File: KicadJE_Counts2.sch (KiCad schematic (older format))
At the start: 40 parts, among them J201 clk_in, J202 clk_out, J203 Hold, J204 Reset, J205 Slave clock sel, P201 HEADER_2x5_Doepfer, U201 LM555, U202 4017

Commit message: counter fine
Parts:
- removed C201: 22u, Capacitor_SMD:C_1206_3216Metric_Pad1.42x1.75mm_HandSolder, symbol Device:C
- removed C202: 10n, AJ:C_0805_AJ, symbol Device:C
- removed R201: 3k3, AJ:R_0805_AJ, symbol Device:R
- removed R202: 220k, AJ:R_0805_AJ, symbol Device:R
- removed RV201: 50k Rate, Connector_JST:JST_EH_B3B-EH-A_1x03_P2.50mm_Vertical, symbol Device:R_POT
- removed U201: LM555, AJ-Dropbox-Kicad:AJ_SO-8_5.3x6.2mm_P1.27mm, symbol KicadJE_SympleSeq-rescue:LM555-Timer
- added C?: 10n, Capacitor_SMD:C_0805_2012Metric_Pad1.15x1.40mm_HandSolder, symbol Device:C
- added C?: 10u, Capacitor_SMD:C_0805_2012Metric_Pad1.15x1.40mm_HandSolder, symbol Device:C
- added R?: 3k3, Resistor_SMD:R_0805_2012Metric_Pad1.15x1.40mm_HandSolder, symbol Device:R
- added R?: 220k, Resistor_SMD:R_0805_2012Metric_Pad1.15x1.40mm_HandSolder, symbol Device:R
- added RV?: 50k_freq, Potentiometer_THT:Potentiometer_China_RK09_Single_Vertical_AJ, symbol Device:R_POT
- added U?: LM555, AJ-Dropbox-Kicad:AJ_SO-8_5.3x6.2mm_P1.27mm, symbol KicadJE_Counts-rescue:LM555-Timer
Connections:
- net labels added: GNDS
- wire segments 166 -> 168
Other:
- moved on the sheet: C203, C204, C205, C206, C207, D201, D202, D203, D204, D205, D206, D207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

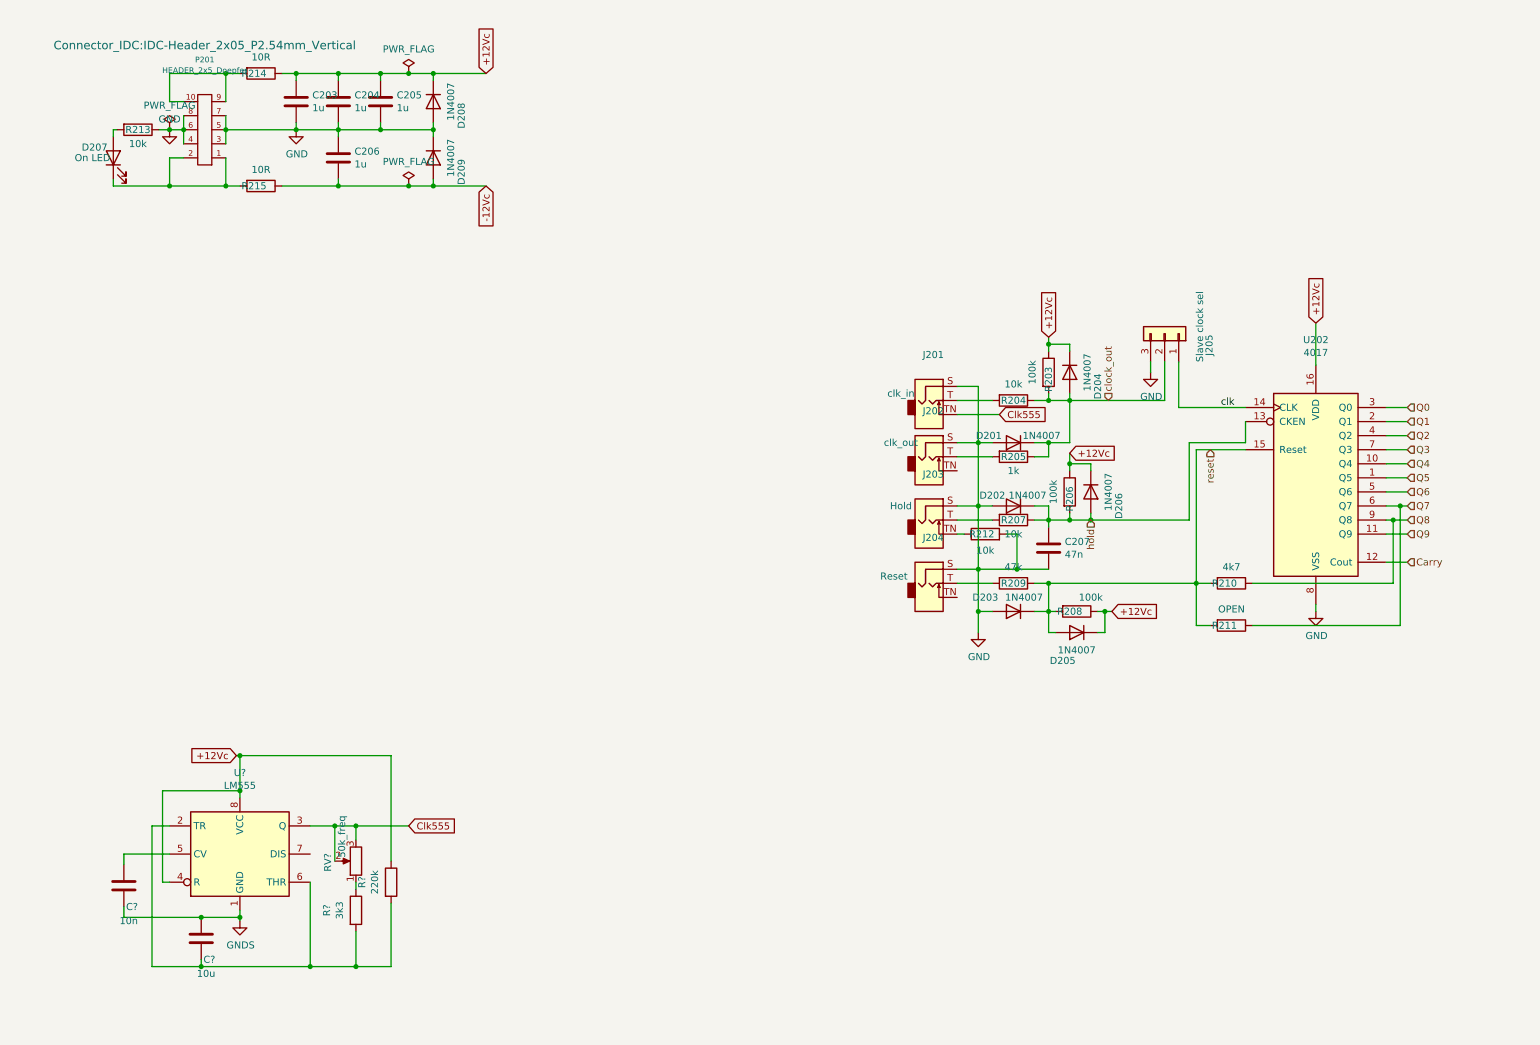
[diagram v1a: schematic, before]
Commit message: distortion added as count2
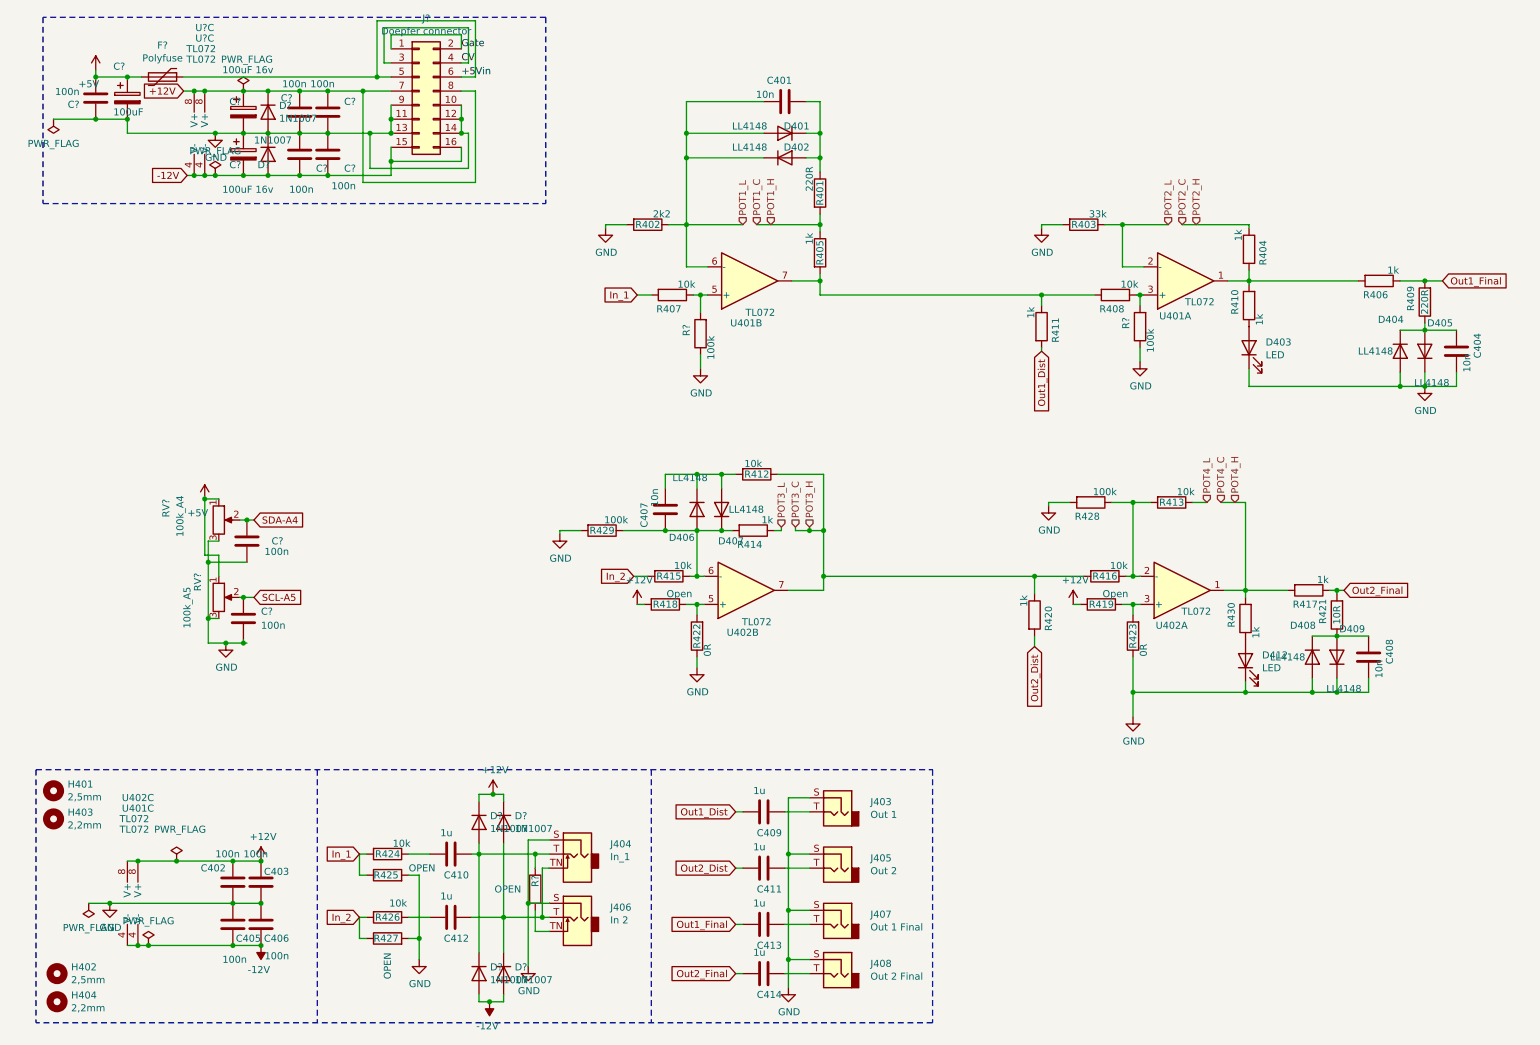
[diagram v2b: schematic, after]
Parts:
- removed C203, C205: 1u, AJ:C_0805_AJ, symbol Device:C
- removed C204, C206: 1u, Capacitor_SMD:C_1206_3216Metric_Pad1.42x1.75mm_HandSolder, symbol Device:C
- removed C207: 47n, AJ:C_0805_AJ, symbol Device:C
- removed C?: 10n, Capacitor_SMD:C_0805_2012Metric_Pad1.15x1.40mm_HandSolder, symbol Device:C
- removed C?: 10u, Capacitor_SMD:C_0805_2012Metric_Pad1.15x1.40mm_HandSolder, symbol Device:C
- removed D201, D202, D203, D204, D205, D206, D208, D209: 1N4007, Diode_SMD:D_MiniMELF, symbol Diode:LL4148
- removed D207: On LED, AJ:D_0805_AJ, symbol Device:LED
- removed J201: clk_in, Connector_Audio:Jack_3.5mm_Ledino_KB3SPRS_Horizontal, symbol Connector:AudioJack2_SwitchT
- removed J202: clk_out, Connector_Audio:Jack_3.5mm_Ledino_KB3SPRS_Horizontal, symbol Connector:AudioJack2_SwitchT
- removed J203: Hold, Connector_Audio:Jack_3.5mm_Ledino_KB3SPRS_Horizontal, symbol Connector:AudioJack2_SwitchT
- removed J204: Reset, Connector_Audio:Jack_3.5mm_Ledino_KB3SPRS_Horizontal, symbol Connector:AudioJack2_SwitchT
- removed J205: Slave clock sel, Connector_PinHeader_2.54mm:PinHeader_1x03_P2.54mm_Vertical, symbol Connector_Generic:Conn_01x03
- removed P201: HEADER_2x5_Doepfer, Connector_IDC:IDC-Header_2x05_P2.54mm_Vertical, symbol Eurorack:HEADER_2x5_Doepfer
- removed R203, R206, R208: 100k, AJ:R_0805_AJ, symbol Device:R
- removed R204, R207, R212, R213: 10k, AJ:R_0805_AJ, symbol Device:R
- removed R205: 1k, AJ:R_0805_AJ, symbol Device:R
- removed R209: 47k, AJ:R_0805_AJ, symbol Device:R
- removed R210: 4k7, AJ:R_0805_AJ, symbol Device:R
- removed R211: OPEN, AJ:R_0805_AJ, symbol Device:R
- removed R214, R215: 10R, AJ:R_0805_AJ, symbol Device:R
- removed R?: 3k3, Resistor_SMD:R_0805_2012Metric_Pad1.15x1.40mm_HandSolder, symbol Device:R
- removed R?: 220k, Resistor_SMD:R_0805_2012Metric_Pad1.15x1.40mm_HandSolder, symbol Device:R
- removed RV?: 50k_freq, Potentiometer_THT:Potentiometer_China_RK09_Single_Vertical_AJ, symbol Device:R_POT
- removed U202: 4017, AJ:SOIC-16_4.55x10.3mm_P1.27mm, symbol 4xxx:4017
- removed U?: LM555, AJ-Dropbox-Kicad:AJ_SO-8_5.3x6.2mm_P1.27mm, symbol KicadJE_Counts-rescue:LM555-Timer
- added C401, C404, C407, C408: 10n, Capacitor_SMD:C_0805_2012Metric_Pad1.15x1.40mm_HandSolder, symbol Device:C
- added C402, C403, C405, C406, C? (x7): 100n, Capacitor_SMD:C_0805_2012Metric_Pad1.15x1.40mm_HandSolder, symbol Device:C
- added C409, C410, C411, C412, C413, C414: 1u, Capacitor_SMD:C_0805_2012Metric_Pad1.15x1.40mm_HandSolder, symbol Device:C
- added C? (x2): 100uF 16v, Capacitor_THT:CP_Radial_D5.0mm_P2.50mm, symbol Device:CP
- added C?: 100uF, Capacitor_THT:CP_Radial_D5.0mm_P2.50mm, symbol Device:CP
- added D401, D402, D404, D405, D406, D407, D408, D409: LL4148, Diode_SMD:D_MiniMELF, symbol Diode:LL4148
- added D403, D412: LED, LED_THT:LED_D3.0mm, symbol Device:LED
- added D? (x6): 1N1007, Diode_SMD:D_SOD-123, symbol Device:D
- added F?: Polyfuse, Fuse:Fuse_1206_3216Metric_Pad1.42x1.75mm_HandSolder, symbol Device:Polyfuse
- added H401, H402: 2,5mm, MountingHole:MountingHole_2.5mm_Pad_Via, symbol Mechanical:MountingHole
- added H403, H404: 2,2mm, MountingHole:MountingHole_2.2mm_M2_Pad_Via, symbol Mechanical:MountingHole
- added J403: Out 1, AJ-Dropbox-Kicad:PJ301SM, symbol Connector:AudioJack2
- added J404: In_1, AJ-Dropbox-Kicad:PJ301SM, symbol Connector:AudioJack2_SwitchT
- added J405: Out 2, AJ-Dropbox-Kicad:PJ301SM, symbol Connector:AudioJack2
- added J406: In 2, AJ-Dropbox-Kicad:PJ301SM, symbol Connector:AudioJack2_SwitchT
- added J407: Out 1 Final, AJ-Dropbox-Kicad:PJ301SM, symbol Connector:AudioJack2
- added J408: Out 2 Final, AJ-Dropbox-Kicad:PJ301SM, symbol Connector:AudioJack2
- added J?: Doepfer connector, Connector_PinSocket_2.54mm:PinSocket_2x08_P2.54mm_Vertical, symbol Connector_Generic:Conn_02x08_Odd_Even
- added R401, R409: 220R, Resistor_SMD:R_0805_2012Metric_Pad1.15x1.40mm_HandSolder, symbol Device:R
- added R402: 2k2, Resistor_SMD:R_0805_2012Metric_Pad1.15x1.40mm_HandSolder, symbol Device:R
- added R403: 33k, Resistor_SMD:R_0805_2012Metric_Pad1.15x1.40mm_HandSolder, symbol Device:R
- added R404, R405, R406, R410, R411, R414, R417, R420, R430: 1k, Resistor_SMD:R_0805_2012Metric_Pad1.15x1.40mm_HandSolder, symbol Device:R
- added R407, R408, R412, R413, R415, R416, R424, R426: 10k, Resistor_SMD:R_0805_2012Metric_Pad1.15x1.40mm_HandSolder, symbol Device:R
- added R418, R419: Open, Resistor_SMD:R_0805_2012Metric_Pad1.15x1.40mm_HandSolder, symbol Device:R
- added R421: 10R, Resistor_SMD:R_0805_2012Metric_Pad1.15x1.40mm_HandSolder, symbol Device:R
- added R422, R423: 0R, Resistor_SMD:R_0805_2012Metric_Pad1.15x1.40mm_HandSolder, symbol Device:R
- added R425, R427, R?: OPEN, Resistor_SMD:R_0805_2012Metric_Pad1.15x1.40mm_HandSolder, symbol Device:R
- added R428, R429, R? (x2): 100k, Resistor_SMD:R_0805_2012Metric_Pad1.15x1.40mm_HandSolder, symbol Device:R
- added RV?: 100k_A4, Potentiometer_THT:Potentiometer_China_RK09_Single_Vertical_AJ, symbol Device:R_POT
- added RV?: 100k_A5, Potentiometer_THT:Potentiometer_China_RK09_Single_Vertical_AJ, symbol Device:R_POT
- added U401, U402, U? (x2): TL072, AJ-Dropbox-Kicad:AJ_SO-8_5.3x6.2mm_P1.27mm, symbol Amplifier_Operational:TL072
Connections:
- net GND: now also C402.1, C403.1, C404.2, C405.2, C406.2, C408.2, C?.1, C?.1, C?.1, C?.1, C?.2, C?.2, C?.2, C?.2, C?.2, C?.2, D403.1 (K), D404.2 (A), D405.1 (K), D408.2 (A), D409.1 (K), D412.1 (K), D?.1 (K), D?.2 (A), J403.S, J404.S, J405.S, J406.S, J407.S, J408.S, J?.10 (Pin_10), J?.11 (Pin_11), J?.12 (Pin_12), J?.13 (Pin_13), J?.14 (Pin_14), J?.9 (Pin_9), R402.2, R403.2, R422.1, R423.1, R425.2, R427.2, R428.2, R429.2, R?.1, R?.1, RV?.3, RV?.3
- new net: R404.2, R406.2, R410.2, U401.1
- new net: R408.1, R?.2, U401.3 (+)
- new net: R407.1, R?.2, U401.5 (+)
- new net: R405.2, R408.2, R411.1, U401.7
- new net: C409.1, J403.T
- new net: C411.1, J405.T
- new net: C410.1, D?.1 (K), D?.2 (A), J404.T, R?.1
- new net: C412.1, D?.1 (K), D?.2 (A), J404.TN, J406.T
- new net: C410.2, R424.1
- new net: C412.2, R426.1
- new net: J406.TN, R?.2
- new net: C414.1, J408.T
- new net: R413.2, R416.1, R428.1, U402.2 (-)
- new net: R419.1, R423.2, U402.3 (+)
- new net: R418.1, R422.2, U402.5 (+)
- new net: C407.1, D406.2 (A), D407.1 (K), R414.2, R415.1, R429.1, U402.6 (-)
- new net: C407.2, D406.1 (K), D407.2 (A), R412.2
- new net: C413.1, J407.T
- new net: C408.1, D408.1 (K), D409.2 (A), R421.1
- new net: C401.2, D401.1 (K), D402.2 (A), R401.1
- new net: C404.1, D404.1 (K), D405.2 (A), R409.1
- new net: D403.2 (A), R410.1
- new net: D412.2 (A), R430.1
- new net +12V: C402.2, C403.2, C?.1, C?.2, C?.2, D?.1 (K), D?.1 (K), D?.1 (K), J?.7 (Pin_7), J?.8 (Pin_8), R418.2, R419.2, U401.8 (V+), U402.8 (V+), U?.8 (V+), U?.8 (V+)
- new net +5V: C?.1, C?.2, F?.2, RV?.1, RV?.1
- new net +5Vin: F?.1, J?.5 (Pin_5), J?.6 (Pin_6)
- new net -12V: C405.1, C406.1, C?.1, C?.1, C?.2, D?.2 (A), D?.2 (A), D?.2 (A), J?.15 (Pin_15), J?.16 (Pin_16), U401.4 (V-), U402.4 (V-), U?.4 (V-), U?.4 (V-)
- new net CV: J?.3 (Pin_3), J?.4 (Pin_4)
- new net Gate: J?.1 (Pin_1), J?.2 (Pin_2)
- new net In_1: R407.2, R424.2, R425.1
- new net In_2: R415.2, R426.2, R427.1
- new net Out1_Dist: C409.2, R411.2
- new net Out1_Final: C413.2, R406.1, R409.2
- new net Out2_Dist: C411.2, R420.2
- new net Out2_Final: C414.2, R417.1, R421.2
- new net POT1_C: R401.2, R405.1
- new net POT1_L: C401.1, D401.2 (A), D402.1 (K), R402.1, U401.6 (-)
- new net POT2_C: R404.1
- new net POT2_L: R403.1, U401.2 (-)
- new net POT3_C: R412.1, R416.2, R420.1, U402.7
- new net POT3_L: R414.1
- new net POT4_C: R417.2, R430.2, U402.1
- new net POT4_L: R413.1
- new net SCL-A5: C?.1, RV?.2
- new net SDA-A4: C?.1, RV?.2

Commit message: Update KicadJE_Counts2.sch
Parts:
- removed C? (x2): 100n, Capacitor_SMD:C_0805_2012Metric_Pad1.15x1.40mm_HandSolder, symbol Device:C
- removed RV?: 100k_A5, Potentiometer_THT:Potentiometer_China_RK09_Single_Vertical_AJ, symbol Device:R_POT
- added RV? (x3): 100k_A4, Potentiometer_THT:Potentiometer_China_RK09_Single_Vertical_AJ, symbol Device:R_POT
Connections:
- net SDA-A4 is gone; now on net POT3_C: RV?.2
- net +5V: no longer RV?.1
- net GND: no longer RV?.3
- net POT3_C: now also RV?.3, RV?.2, RV?.3
- net POT4_C: now also RV?.2, RV?.2, RV?.3, RV?.3
- net POT4_L: now also RV?.1, RV?.1
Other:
- moved on the sheet: RV?
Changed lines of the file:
@@
 Wire Wire Line
 	3800 6100 3875 6100
-Text GLabel 2100 4700 2    50   Input ~ 0
-SCL-A5
-Text GLabel 2100 4150 2    50   Input ~ 0
-SDA-A4
 $Comp
 L Device:R_POT RV?
 U 1 1 5F13A9C4
-P 1850 4150
+P 2950 4400
 AR Path="/5F13A9C4" Ref="RV?"  Part="1"
 AR Path="/5D60ED9A/5F13A9C4" Ref="RV?"  Part="1"
-F 0 "RV?" V 1475 4300 50  0000 R CNN
-F 1 "100k_A4" V 1575 4325 50  0000 R CNN
-F 2 "Potentiometer_THT:Potentiometer_China_RK09_Single_Vertical_AJ" H 1850 4150 50  0001 C CNN
-F 3 "~" H 1850 4150 50  0001 C CNN
-	1    1850 4150
-	1    0    0    -1
-$EndComp
-Wire Wire Line
-	2000 4150 2050 4150
-$Comp
-L Device:R_POT RV?
-U 1 1 5F13A9CB
-P 1850 4700
-AR Path="/5F13A9CB" Ref="RV?"  Part="1"
-AR Path="/5D60ED9A/5F13A9CB" Ref="RV?"  Part="1"
-F 0 "RV?" V 1700 4875 50  0000 R CNN
-F 1 "100k_A5" V 1625 4775 50  0000 R CNN
-F 2 "Potentiometer_THT:Potentiometer_China_RK09_Single_Vertical_AJ" H 1850 4700 50  0001 C CNN
-F 3 "~" H 1850 4700 50  0001 C CNN
-	1    1850 4700
-	1    0    0    -1
-$EndComp
-Wire Wire Line
-	2000 4700 2025 4700
-Wire Wire Line
-	1750 4400 1750 4000
-Wire Wire Line
-	1750 4000 1850 4000
-Wire Wire Line
-	1775 4850 1850 4850
-$Comp
-L power:GND #PWR?
-U 1 1 5F13A9D5
-P 1900 5025
-AR Path="/5F13A9D5" Ref="#PWR?"  Part="1"
-AR Path="/5D60ED9A/5F13A9D5" Ref="#PWR?"  Part="1"
-F 0 "#PWR?" H 1900 4775 50  0001 C CNN
-F 1 "GND" H 1905 4852 50  0000 C CNN
-F 2 "" H 1900 5025 50  0001 C CNN
-F 3 "" H 1900 5025 50  0001 C CNN
-	1    1900 5025
-	1    0    0    -1
-$EndComp
-$Comp
-L power:+5V #PWR?
-U 1 1 5F13A9DB
-P 1750 4000
-AR Path="/5F13A9DB" Ref="#PWR?"  Part="1"
-AR Path="/5D60ED9A/5F13A9DB" Ref="#PWR?"  Part="1"
-F 0 "#PWR?" H 1750 3850 50  0001 C CNN
-F 1 "+5V" H 1700 3900 50  0000 C CNN
-F 2 "" H 1750 4000 50  0001 C CNN
-F 3 "" H 1750 4000 50  0001 C CNN
-	1    1750 4000
-	1    0    0    -1
-$EndComp
-Connection ~ 1750 4000
-$Comp
-L Device:C C?
-U 1 1 5F13A9E2
-P 2025 4850
-AR Path="/5F13A9E2" Ref="C?"  Part="1"
-AR Path="/5D60ED9A/5F13A9E2" Ref="C?"  Part="1"
-F 0 "C?" H 2150 4900 50  0000 L CNN
-F 1 "100n" H 2150 4800 50  0000 L CNN
-F 2 "Capacitor_SMD:C_0805_2012Metric_Pad1.15x1.40mm_HandSolder" H 2063 4700 50  0001 C CNN
-F 3 "~" H 2025 4850 50  0001 C CNN
-	1    2025 4850
-	1    0    0    -1
-$EndComp
-Connection ~ 2025 4700
-Wire Wire Line
-	2025 4700 2100 4700
-Wire Wire Line
-	1775 4850 1775 5025
-Wire Wire Line
-	1775 5025 1900 5025
-Wire Wire Line
-	2025 5025 2025 5000
-Connection ~ 1900 5025
-Wire Wire Line
-	1900 5025 2025 5025
-$Comp
-L Device:C C?
-U 1 1 5F13A9EF
-P 2050 4300
-AR Path="/5F13A9EF" Ref="C?"  Part="1"
-AR Path="/5D60ED9A/5F13A9EF" Ref="C?"  Part="1"
-F 0 "C?" H 2225 4300 50  0000 L CNN
-F 1 "100n" H 2175 4225 50  0000 L CNN
-F 2 "Capacitor_SMD:C_0805_2012Metric_Pad1.15x1.40mm_HandSolder" H 2088 4150 50  0001 C CNN
-F 3 "~" H 2050 4300 50  0001 C CNN
-	1    2050 4300
-	1    0    0    -1
-$EndComp
-Connection ~ 2050 4150
-Wire Wire Line
-	2050 4150 2100 4150
-Wire Wire Line
-	2050 5025 2025 5025
-Connection ~ 2025 5025
-Wire Wire Line
-	1850 4550 1850 4400
-Wire Wire Line
-	1850 4400 1750 4400
-Wire Wire Line
-	1850 4300 1775 4300
-Wire Wire Line
-	1775 4300 1775 4450
-Connection ~ 1775 4850
-Wire Wire Line
-	2050 4450 1775 4450
-Connection ~ 1775 4450
-Wire Wire Line
-	1775 4450 1775 4850
+F 0 "RV?" V 2575 4550 50  0000 R CNN
+F 1 "100k_A4" V 2675 4575 50  0000 R CNN
+F 2 "Potentiometer_THT:Potentiometer_China_RK09_Single_Vertical_AJ" H 2950 4400 50  0001 C CNN
+F 3 "~" H 2950 4400 50  0001 C CNN
+	1    2950 4400
+	1    0    0    1
+$EndComp
 $Comp
 L Device:C C?
@@
 Wire Notes Line
 	600  1900 4175 1900
+Text HLabel 3250 4225 2    50   Input ~ 0
+POT3_H
+Text HLabel 3250 4400 2    50   Input ~ 0
+POT3_C
+Text HLabel 3250 4575 2    50   Input ~ 0
+POT3_L
+Text HLabel 3250 4775 2    50   Input ~ 0
+POT4_H
+Text HLabel 3250 4925 2    50   Input ~ 0
+POT4_C
+Text HLabel 3250 5075 2    50   Input ~ 0
+POT4_L
+$Comp
+L Device:R_POT RV?
+U 1 1 5F31783B
+P 2950 4925
+AR Path="/5F31783B" Ref="RV?"  Part="1"
+AR Path="/5D60ED9A/5F31783B" Ref="RV?"  Part="1"
+F 0 "RV?" V 2575 5075 50  0000 R CNN
+F 1 "100k_A4" V 2675 5100 50  0000 R CNN
+F 2 "Potentiometer_THT:Potentiometer_China_RK09_Single_Vertical_AJ" H 2950 4925 50  0001 C CNN
+F 3 "~" H 2950 4925 50  0001 C CNN
+	1    2950 4925
+	1    0    0    1
+$EndComp
+Wire Wire Line
+	2950 4775 3250 4775
+Wire Wire Line
+	3100 4925 3250 4925
+Wire Wire Line
+	2950 5075 3250 5075
+Wire Wire Line
+	3225 4575 2950 4575
+Wire Wire Line
+	2950 4575 2950 4550
+Wire Wire Line
+	2950 4250 2950 4225
+Wire Wire Line
+	2950 4225 3250 4225
+Wire Wire Line
+	3100 4400 3250 4400
+$Comp
+L Device:R_POT RV?
+U 1 1 5F3F817E
+P 2950 2825
+AR Path="/5F3F817E" Ref="RV?"  Part="1"
+AR Path="/5D60ED9A/5F3F817E" Ref="RV?"  Part="1"
+F 0 "RV?" V 2575 2975 50  0000 R CNN
+F 1 "100k_A4" V 2675 3000 50  0000 R CNN
+F 2 "Potentiometer_THT:Potentiometer_China_RK09_Single_Vertical_AJ" H 2950 2825 50  0001 C CNN
+F 3 "~" H 2950 2825 50  0001 C CNN
+	1    2950 2825
+	1    0    0    1
+$EndComp
+Text HLabel 3250 2650 2    50   Input ~ 0
+POT3_H
+Text HLabel 3250 2825 2    50   Input ~ 0
+POT3_C
+Text HLabel 3250 3000 2    50   Input ~ 0
+POT3_L
+Text HLabel 3250 3200 2    50   Input ~ 0
+POT4_H
+Text HLabel 3250 3350 2    50   Input ~ 0
+POT4_C
+Text HLabel 3250 3500 2    50   Input ~ 0
+POT4_L
+$Comp
+L Device:R_POT RV?
+U 1 1 5F3F818E
+P 2950 3350
+AR Path="/5F3F818E" Ref="RV?"  Part="1"
+AR Path="/5D60ED9A/5F3F818E" Ref="RV?"  Part="1"
+F 0 "RV?" V 2575 3500 50  0000 R CNN
+F 1 "100k_A4" V 2675 3525 50  0000 R CNN
+F 2 "Potentiometer_THT:Potentiometer_China_RK09_Single_Vertical_AJ" H 2950 3350 50  0001 C CNN
+F 3 "~" H 2950 3350 50  0001 C CNN
+	1    2950 3350
+	1    0    0    1
+$EndComp
+Wire Wire Line
+	2950 3200 3250 3200
+Wire Wire Line
+	3100 3350 3250 3350
+Wire Wire Line
+	2950 3500 3250 3500
+Wire Wire Line
+	3225 3000 2950 3000
+Wire Wire Line
+	2950 3000 2950 2975
+Wire Wire Line
+	2950 2675 2950 2650
+Wire Wire Line
+	2950 2650 3250 2650
+Wire Wire Line
+	3100 2825 3250 2825
 $EndSCHEMATC

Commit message: sch updates
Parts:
- gave numbers to parts that had none: 25
- renumbered C402 to C303, C405 to C304, C403 to C307, C406 to C308, C410 to C313, C412 to C314, C407 to C315, C409 to C316, C411 to C317, C413 to C318, C414 to C319, C401 to C320, C408 to C321, C404 to C322, D406 to D307, D407 to D308, D401 to D309, D402 to D310, D412 to D311, D403 to D312, D408 to D313, D409 to D314, D404 to D315, D405 to D316, H401 to H301, H403 to H302, H402 to H303, H404 to H304, J404 to J302, J406 to J303, J403 to J304, J405 to J305, J407 to J306, J408 to J307, R424 to R301, R425 to R302, R426 to R303, R427 to R304, R429 to R306, R402 to R307, R418 to R308, R415 to R309, R407 to R310, R422 to R311, R414 to R313, R412 to R314, R401 to R315, R405 to R316, R420 to R317, R411 to R318, R403 to R319, R428 to R320, R419 to R321, R416 to R322, R408 to R323, R423 to R324, R413 to R326, R430 to R327, R404 to R328, R410 to R329, R417 to R330, R421 to R331, R406 to R332, R409 to R333, U401 to U301, U402 to U301, U402 to U302, U401 to U302

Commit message: footprint updates
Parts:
- C301, C303, C304, C307, C308, C309, C310, C311, C312, C313, C314, C315, C316, C317, C318, C319, C320, C321, C322: footprint Capacitor_SMD:C_0805_2012Metric_Pad1.15x1.40mm_HandSolder -> AJ:C_0805_AJ
- C302, C305, C306: footprint Capacitor_THT:CP_Radial_D5.0mm_P2.50mm -> Capacitor_SMD:C_1206_3216Metric
- D301, D302, D303, D304, D305, D306: footprint Diode_SMD:D_SOD-123 -> AJ:D_SOD-123
- D307, D308, D309, D310, D313, D314, D315, D316: footprint Diode_SMD:D_MiniMELF -> AJ:D_MiniMELF
- R301, R302, R303, R304, R305, R306, R307, R308, R309, R310, R311, R312, R313, R314, R315, R316, R317, R318, R319, R320, R321, R322, R323, R324, R325, R326, R327, R328, R329, R330, R331, R332, R333: footprint Resistor_SMD:R_0805_2012Metric_Pad1.15x1.40mm_HandSolder -> AJ:R_0805_AJ

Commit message: Update KicadJE_Counts2.sch
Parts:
- removed C301, C303, C304, C307, C308: 100n, AJ:C_0805_AJ, symbol Device:C
- removed C302: 100uF, Capacitor_SMD:C_1206_3216Metric, symbol Device:CP
- removed F301: Polyfuse, Fuse:Fuse_1206_3216Metric_Pad1.42x1.75mm_HandSolder, symbol Device:Polyfuse
- removed unit 3 of U301
- removed unit 3 of U302
- renumbered U303 to U301, U304 to U302
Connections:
- net +5Vin is gone; now on net +5V: J301.5 (Pin_5), J301.6 (Pin_6)
